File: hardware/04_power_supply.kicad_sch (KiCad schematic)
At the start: 0 parts

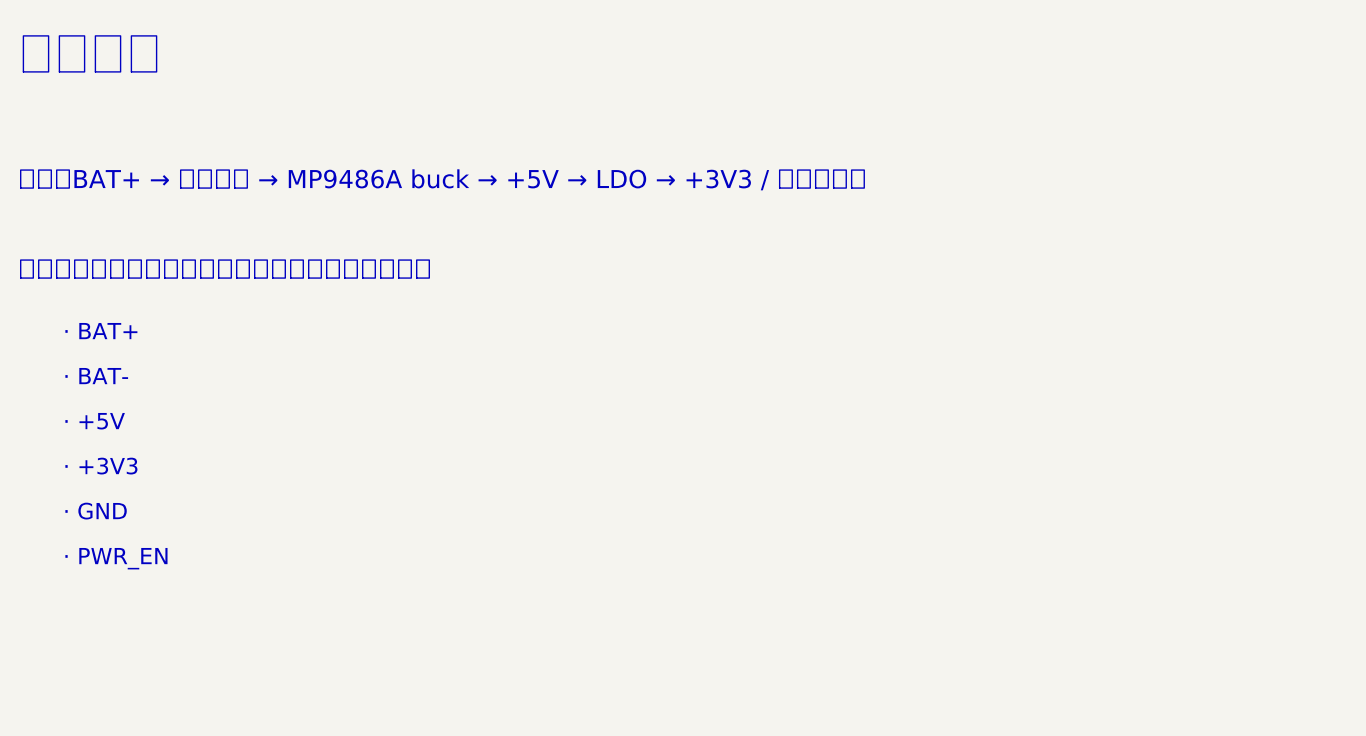
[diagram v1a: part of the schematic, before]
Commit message: 电源改为 LMR16006X 直降 3.3V + SN65HVD230（取消 5V 轨与 LDO）；会话交接文档与技能转移包
- BOM/详细设计/骨架：MP9486A+MP2013A+TJA1051 → LMR16006XDDCR(C87080)+SS210(C14996)+SN65HVD230DR(C12084)
- 成本（元器件）：10 块 ¥393→¥359/块，100 块 ¥294→¥267/块
- docs/00-会话交接.md：新会话的环境恢复、技能恢复、DeepSeek 画图方配置与待办
- transfer/pcb-workflow-skill.tar.gz：云主机上改写的 pcb-workflow 技能（仅用于转移）

Co-Authored-By: Claude Opus 5.5 <noreply@anthropic.com>
Claude-Session: https://claude.ai/code/session_01EyFjq1nqLUmfVYESj2uYXd
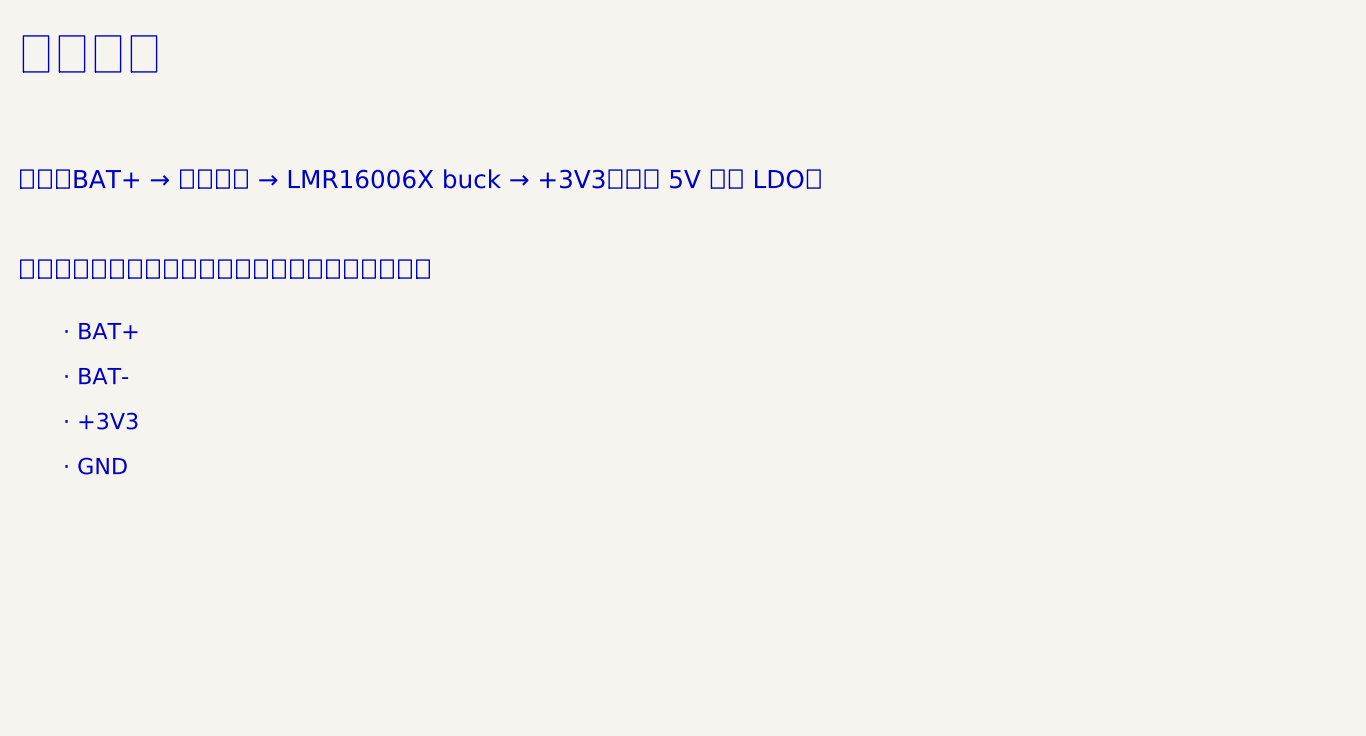
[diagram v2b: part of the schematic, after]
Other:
- note added: "内容：BAT+ → 输入保护 → LMR16006X buck → +3V3（取消 5V 轨与 LDO）"
- note removed: "· +5V"
- note removed: "· PWR_EN"
- note removed: "内容：BAT+ → 输入保护 → MP9486A buck → +5V → LDO → +3V3 / 唤醒与休眠"
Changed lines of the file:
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@@
 		)
 	)
-	(text "内容：BAT+ → 输入保护 → MP9486A buck → +5V → LDO → +3V3 / 唤醒与休眠"
+	(text "内容：BAT+ → 输入保护 → LMR16006X buck → +3V3（取消 5V 轨与 LDO）"
 		(exclude_from_sim no)
 		(at 20 35 0)
@@
 		)
 	)
-	(text "· +5V"
+	(text "· +3V3"
 		(exclude_from_sim no)
 		(at 25 62 0)
@@
 		)
 	)
-	(text "· +3V3"
+	(text "· GND"
 		(exclude_from_sim no)
 		(at 25 67 0)
 		(effects
 			(font
-				(size 1.8 1.8)
-			)
-			(justify left top)
-		)
-	)
-	(text "· GND"
-		(exclude_from_sim no)
-		(at 25 72 0)
-		(effects
-			(font
-				(size 1.8 1.8)
-			)
-			(justify left top)
-		)
-	)
-	(text "· PWR_EN"
-		(exclude_from_sim no)
-		(at 25 77 0)
-		(effects
-			(font

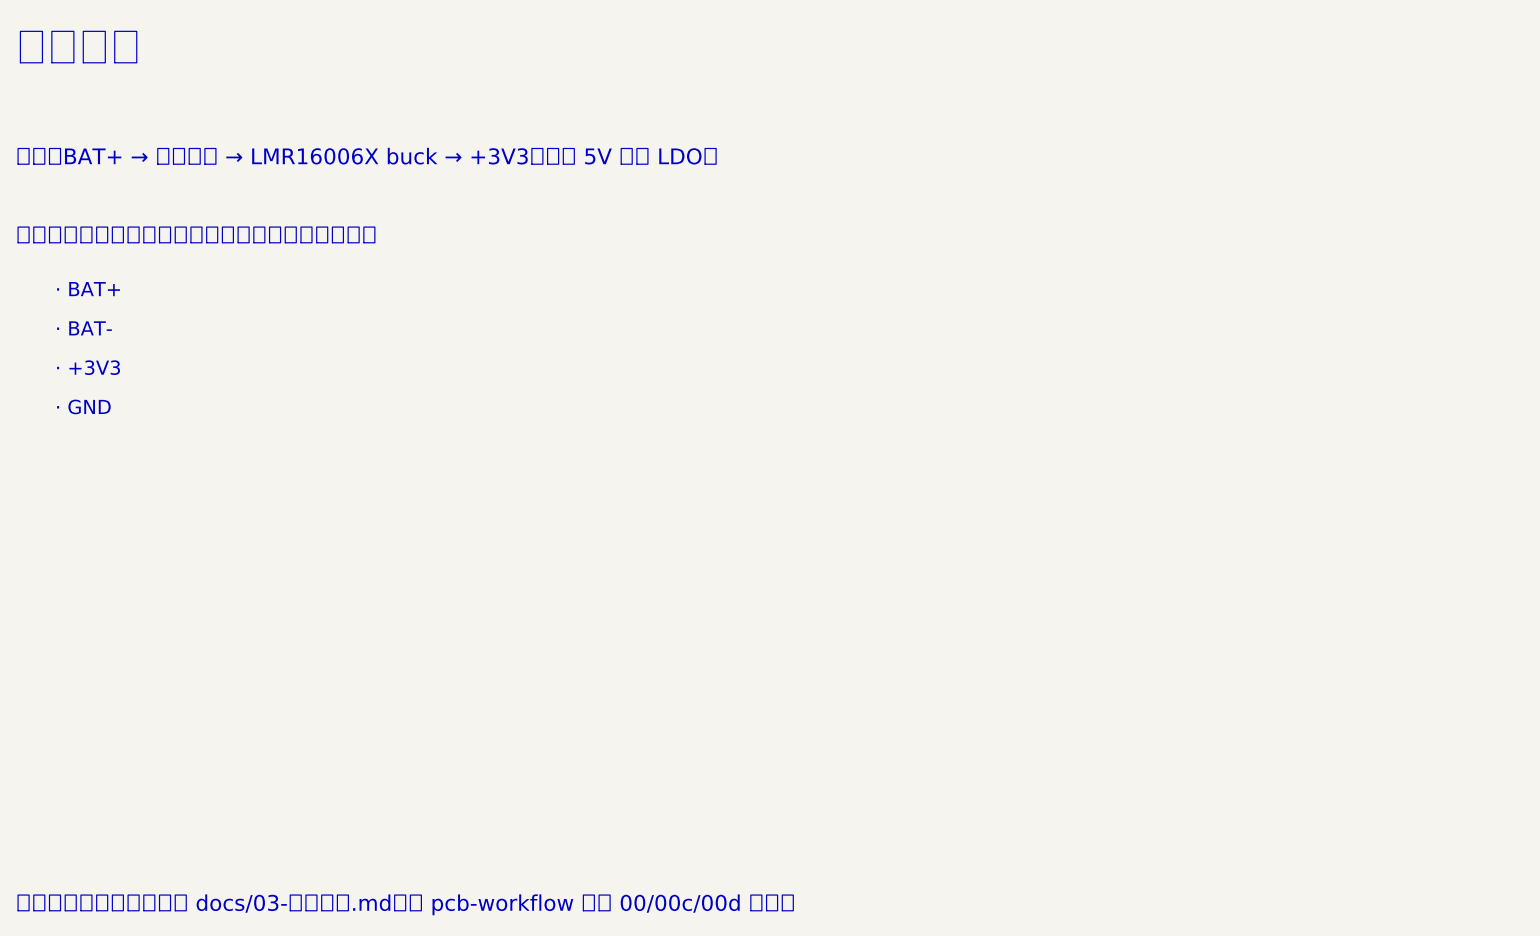
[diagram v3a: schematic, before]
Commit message: 04 子图第 1 轮（DeepSeek 画图，ERC 0 错误）；jlc 库引脚类型统一 passive；第 2 轮任务书（lib_id 加 jlc: 前缀、位号统一）
Co-Authored-By: Claude Opus 5.5 <noreply@anthropic.com>
Claude-Session: https://claude.ai/code/session_018LcBBXJnjJ1MVmds7Fkezv
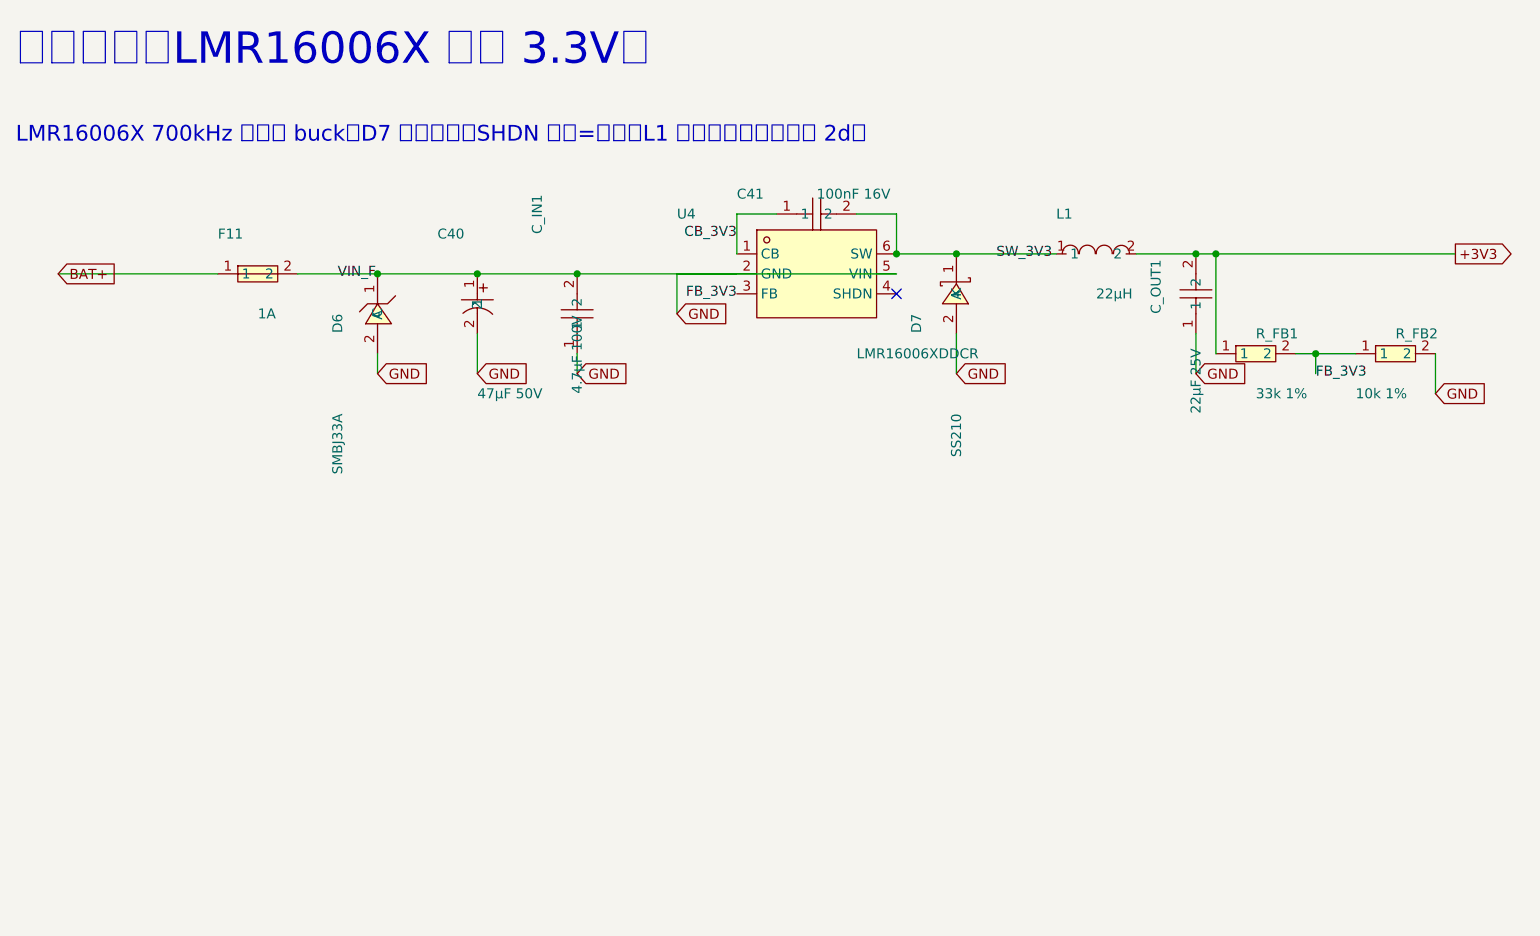
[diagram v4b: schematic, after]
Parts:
- added C40: 47µF 50V, symbol EEE-FT1H470AP
- added C41: 100nF 16V, symbol CL05B104KO5NNNC
- added C_IN1: 4.7µF 100V, symbol FS32X475K101EGG
- added C_OUT1: 22µF 25V, symbol CL21A226MAQNNNE
- added D6: SMBJ33A, symbol SMBJ33A-C78419
- added D7: SS210, symbol SS210
- added F11: 1A, symbol 0466001.NRHF
- added L1: 22µH, symbol SWPA5040S220MT
- added R_FB1: 33k 1%, symbol 0402WGF3302TCE
- added R_FB2: 10k 1%, symbol 0402WGF1002TCE
- added U4: LMR16006XDDCR, symbol LMR16006XDDCR
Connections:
- new net +3V3: C_OUT1.2, L1.2, R_FB1.1
- new net BAT+: F11.1
- new net CB_3V3: C41.1, U4.1 (CB)
- new net FB_3V3: R_FB1.2, R_FB2.1, U4.3 (FB)
- new net GND: C40.1, C40.2, C_IN1.1, C_IN1.2, C_OUT1.1, D6.1 (C), D6.2 (A), D7.2 (A), F11.2, R_FB2.2, U4.2 (GND), U4.5 (VIN)
- new net SW_3V3: C41.2, D7.1 (K), L1.1, U4.6 (SW)
- no-connect marks 0 -> 1
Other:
- note added: "LMR16006X 700kHz 非同步 buck；D7 续流必需；SHDN 悬空=常开；L1 下方全层禁铜（规则 2d）"
- note added: "辅助电源（LMR16006X 直降 3.3V）"
- note removed: "· +3V3"
- note removed: "· BAT+"
- note removed: "· BAT-"
- note removed: "· GND"
- note removed: "内容：BAT+ → 输入保护 → LMR16006X buck → +3V3（取消 5V 轨与 LDO）"
- note removed: "接口网络（跨页用全局标签，名称以本清单为准）："
- note removed: "状态：待画。详细设计见 docs/03-详细设计.md；按 pcb-workflow 规则 00/00c/00d 执行。"
- note removed: "辅助电源"

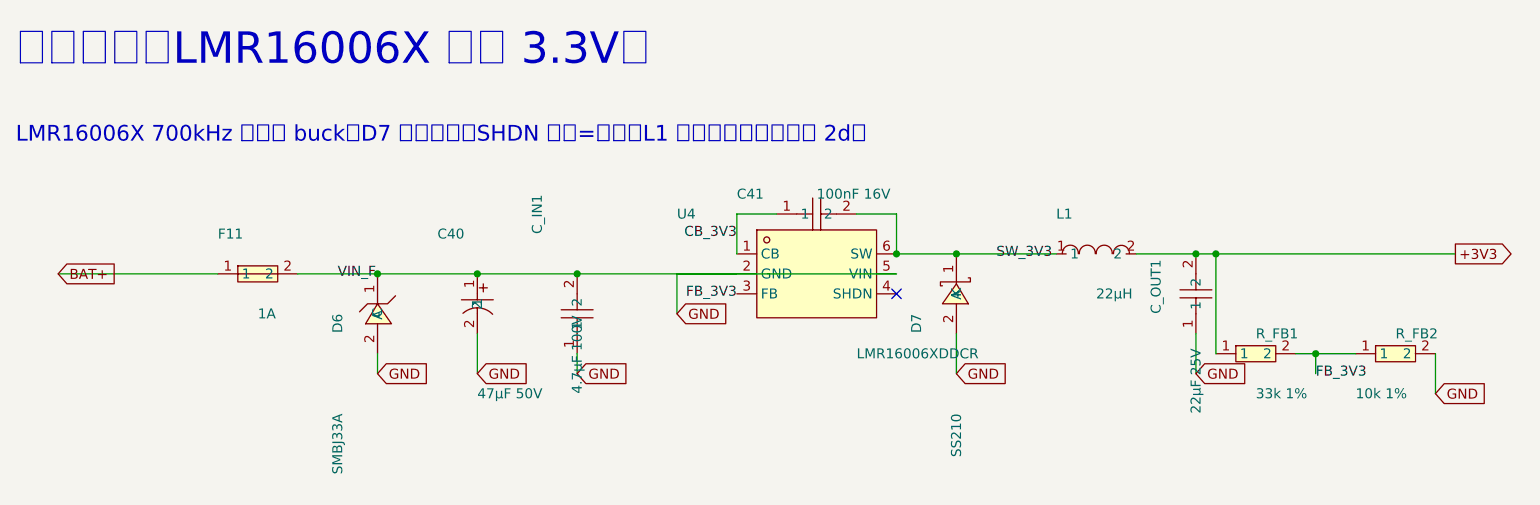
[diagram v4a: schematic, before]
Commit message: 04 子图第 2 轮：lib_id 带 jlc:、位号 C40–C43/R40–R41、删 D6、C40→C48971005；jlc 库用 kicad-cli 升级为当前格式（消 lib_symbol_mismatch 假告警，取库脚本自动做）
Co-Authored-By: Claude Opus 5.5 <noreply@anthropic.com>
Claude-Session: https://claude.ai/code/session_018LcBBXJnjJ1MVmds7Fkezv
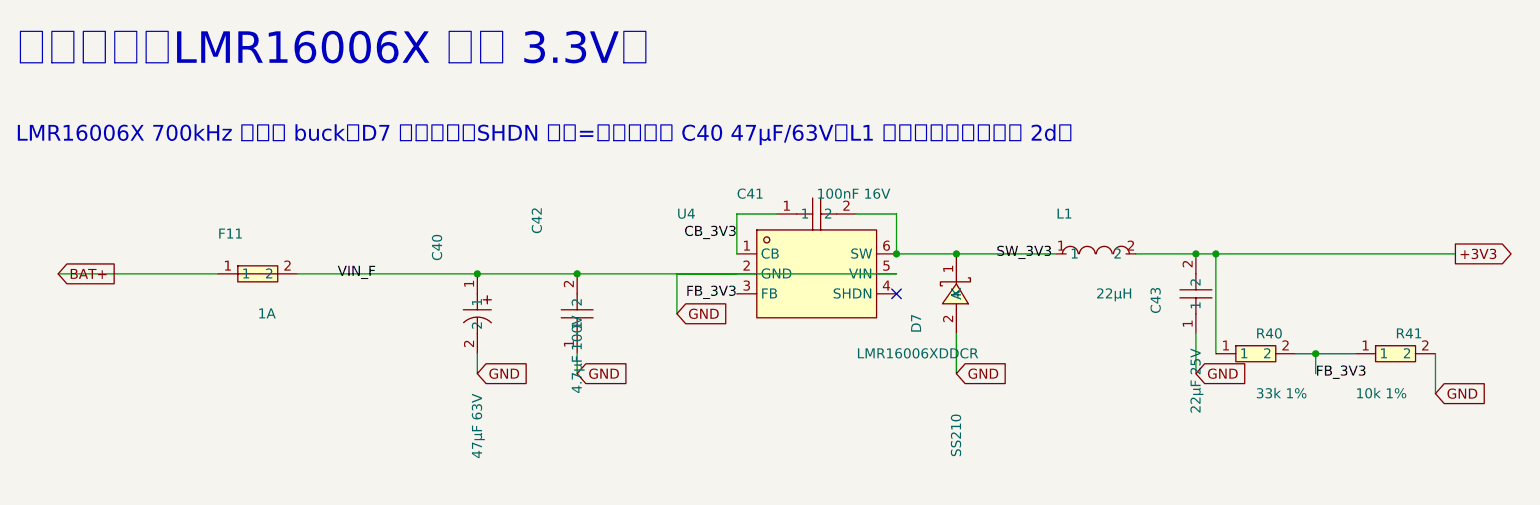
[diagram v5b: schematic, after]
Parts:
- removed C_IN1: 4.7µF 100V, symbol FS32X475K101EGG
- removed C_OUT1: 22µF 25V, symbol CL21A226MAQNNNE
- removed D6: SMBJ33A, symbol SMBJ33A-C78419
- removed R_FB1: 33k 1%, symbol 0402WGF3302TCE
- removed R_FB2: 10k 1%, symbol 0402WGF1002TCE
- added C42: 4.7µF 100V, symbol jlc:FS32X475K101EGG
- added C43: 22µF 25V, symbol jlc:CL21A226MAQNNNE
- added R40: 33k 1%, symbol jlc:0402WGF3302TCE
- added R41: 10k 1%, symbol jlc:0402WGF1002TCE
- C40: value 47µF 50V -> 47µF 63V; symbol EEE-FT1H470AP -> jlc:RV63V47M6X8; LCSC C92059 -> C48971005
- C41: symbol CL05B104KO5NNNC -> jlc:CL05B104KO5NNNC
- D7: symbol SS210 -> jlc:SS210
- F11: symbol 0466001.NRHF -> jlc:0466001.NRHF
- L1: symbol SWPA5040S220MT -> jlc:SWPA5040S220MT
- U4: symbol LMR16006XDDCR -> jlc:LMR16006XDDCR
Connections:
- net +3V3: now also C43.2, R40.1
- net FB_3V3: now also R40.2, R41.1
- net GND: now also C42.1, C42.2, C43.1, R41.2
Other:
- note added: "LMR16006X 700kHz 非同步 buck；D7 续流必需；SHDN 悬空=常开；输入 C40 47µF/63V；L1 下方全层禁铜（规则 2d）"
- note removed: "LMR16006X 700kHz 非同步 buck；D7 续流必需；SHDN 悬空=常开；L1 下方全层禁铜（规则 2d）"
- moved on the sheet: C40
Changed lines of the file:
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@@
 		(title "辅助电源")
 		(date "2026-09-26")
-		(rev "v0.3-draw-r1")
+		(rev "v0.3-draw-r2")
 		(company "MP2645A-BMS")
 		(comment 1 "8S LiFePO4 200A BMS · MPS MP2797 + 开关电容均衡")
@@
 		)
 	)
-	(text "LMR16006X 700kHz 非同步 buck；D7 续流必需；SHDN 悬空=常开；L1 下方全层禁铜（规则 2d）"
+	(text "LMR16006X 700kHz 非同步 buck；D7 续流必需；SHDN 悬空=常开；输入 C40 47µF/63V；L1 下方全层禁铜（规则 2d）"
 		(exclude_from_sim no)
 		(at 20.00 32.00 0)
@@
 	(global_label "GND"
 		(shape input)
-		(at 66.04 63.50 0)
-		(effects
-			(font
-				(size 1.27 1.27)
-			)
-			(justify left)
-		)
-	)
-	(global_label "GND"
-		(shape input)
 		(at 78.74 63.50 0)
 		(effects
@@
 	(wire
 		(pts
-			(xy 66.04 60.96)
-			(xy 66.04 63.50)
-		)
-		(stroke
-			(width 0)
-			(type default)
-		)
-	)
-	(wire
-		(pts
-			(xy 78.74 58.42)
+			(xy 78.74 60.96)
 			(xy 78.74 63.50)
 		)
@@
 		)
 	)
-	(junction (at 66.04 50.80) (diameter 0) (color 0 0 0 0))
 	(junction (at 78.74 50.80) (diameter 0) (color 0 0 0 0))
 	(junction (at 91.44 50.80) (diameter 0) (color 0 0 0 0))
@@
 	(no_connect (at 132.08 53.34))
 	(symbol
-		(lib_id "LMR16006XDDCR")
+		(lib_id "jlc:LMR16006XDDCR")
 		(at 121.92 50.80 0)
 		(unit 1)
@@
 	)
 	(symbol
-		(lib_id "0466001.NRHF")
+		(lib_id "jlc:0466001.NRHF")
 		(at 50.80 50.80 0)
 		(unit 1)
@@
 	)
 	(symbol
-		(lib_id "SMBJ33A-C78419")
-		(at 66.04 55.88 270)
-		(unit 1)
-		(exclude_from_sim no)
-		(in_bom yes)
-		(on_board yes)
-		(dnp no)
-		(property "Reference" "D6"
-			(at 60.96 55.88 0)
-			(effects
-				(font
-					(size 1.27 1.27)
-				)
-				(justify left)
-			)
-		)
-		(property "Value" "SMBJ33A"
-			(at 60.96 68.58 0)
-			(effects
-				(font
-					(size 1.27 1.27)
-				)
-				(justify left)
-			)
-		)
-		(property "LCSC" "C78419"
-			(at 66.04 63.50 0)
-			(effects
-				(font
-					(size 1.27 1.27)
-				)
-				(justify left)
-				hide
-			)
-		)
-		(pin "1")
-		(pin "2")
-		(instances
-			(project "mp2645a-bms"
-				(path "/632f74a5-cd8f-58d8-9ac1-1bfbb611d555/c20e45f9-c9d2-50e9-b477-f2356556af13"
-					(reference "D6")
-					(unit 1)
-				)
-			)
-		)
-	)
-	(symbol
-		(lib_id "EEE-FT1H470AP")
-		(at 78.74 54.61 0)
+		(lib_id "jlc:RV63V47M6X8")
+		(at 78.74 55.88 270)
 		(unit 1)
 		(exclude_from_sim no)
@@
 			)
 		)
-		(property "Value" "47µF 50V"
+		(property "Value" "47µF 63V"
 			(at 78.74 66.04 0)
 			(effects
@@
 			)
 		)
-		(property "LCSC" "C92059"
-			(at 78.74 62.23 0)
+		(property "LCSC" "C48971005"
+			(at 78.74 63.50 0)
 			(effects
 				(font
@@
 	)
 	(symbol
-		(lib_id "FS32X475K101EGG")
+		(lib_id "jlc:FS32X475K101EGG")
 		(at 91.44 55.88 90)
 		(unit 1)
@@
 		(on_board yes)
 		(dnp no)
-		(property "Reference" "C_IN1"
+		(property "Reference" "C42"
 			(at 86.36 45.72 0)
 			(effects
@@
 			(project "mp2645a-bms"
 				(path "/632f74a5-cd8f-58d8-9ac1-1bfbb611d555/c20e45f9-c9d2-50e9-b477-f2356556af13"
-					(reference "C_IN1")
-					(unit 1)
-				)
-			)
-		)
-	)
-	(symbol
-		(lib_id "CL05B104KO5NNNC")
+					(reference "C42")
+					(unit 1)
+				)
+			)
+		)
+	)
+	(symbol
+		(lib_id "jlc:CL05B104KO5NNNC")
 		(at 121.92 43.18 0)
 		(unit 1)
@@
 	)
 	(symbol
-		(lib_id "SS210")
+		(lib_id "jlc:SS210")
 		(at 139.70 53.34 270)
 		(unit 1)
@@
 	)
 	(symbol
-		(lib_id "SWPA5040S220MT")
+		(lib_id "jlc:SWPA5040S220MT")
 		(at 157.48 48.26 0)
 		(unit 1)
@@
 	)
 	(symbol
-		(lib_id "CL21A226MAQNNNE")
+		(lib_id "jlc:CL21A226MAQNNNE")
 		(at 170.18 53.34 90)
 		(unit 1)
@@
 		(on_board yes)
 		(dnp no)
-		(property "Reference" "C_OUT1"
+		(property "Reference" "C43"
 			(at 165.10 55.88 0)
 			(effects
@@
 			(project "mp2645a-bms"
 				(path "/632f74a5-cd8f-58d8-9ac1-1bfbb611d555/c20e45f9-c9d2-50e9-b477-f2356556af13"
-					(reference "C_OUT1")
-					(unit 1)
-				)
-			)
-		)
-	)
-	(symbol
-		(lib_id "0402WGF3302TCE")
+					(reference "C43")
+					(unit 1)
+				)
+			)
+		)
+	)
+	(symbol
+		(lib_id "jlc:0402WGF3302TCE")
 		(at 177.80 60.96 0)
 		(unit 1)
@@
 		(on_board yes)
 		(dnp no)
-		(property "Reference" "R_FB1"
+		(property "Reference" "R40"
 			(at 177.80 58.42 0)
 			(effects
@@
 			(project "mp2645a-bms"
 				(path "/632f74a5-cd8f-58d8-9ac1-1bfbb611d555/c20e45f9-c9d2-50e9-b477-f2356556af13"
-					(reference "R_FB1")
-					(unit 1)
-				)
-			)
-		)
-	)
-	(symbol
-		(lib_id "0402WGF1002TCE")
+					(reference "R40")
+					(unit 1)
+				)
+			)
+		)
+	)
+	(symbol
+		(lib_id "jlc:0402WGF1002TCE")
 		(at 195.58 60.96 0)
 		(unit 1)
@@
 		(on_board yes)
 		(dnp no)
-		(property "Reference" "R_FB2"
+		(property "Reference" "R41"
 			(at 195.58 58.42 0)
 			(effects
@@
 			(project "mp2645a-bms"
 				(path "/632f74a5-cd8f-58d8-9ac1-1bfbb611d555/c20e45f9-c9d2-50e9-b477-f2356556af13"
-					(reference "R_FB2")
-					(unit 1)
-				)
+					(reference "R41")
+					(unit 1)
+				)
